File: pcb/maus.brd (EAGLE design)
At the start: 100 x 101 mm, 79 parts, among them IC1 AP1509-50SG-13, J1 SS-52300-001, Q2 BSS123, Q3 BSS123, Q4 BSS123, Q6 PMN30XPEA, Q7 PMN30XPEA, U2 CH340C, U4 LP3965EMP-3.3, U6 LM358DR, U69 ESP32-S2-WROOM

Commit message: replace old libraries
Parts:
- CR1: device shared:POWERSO-20_STM -> maus:POWERSO-20_STM
- D1: device SP0503BAHTG:SOT143 -> maus:SOT143
- D10, D11, D12, D16, D17, D18, D19, D8, YRMOM: device shared:RB068VWM100 -> maus:RB068VWM100
- IC1: device shared:SOIC127P600X175-8N -> maus:SOIC127P600X175-8N
- J1: device shared:SS52300001 -> maus:SS52300001
- JP1, JP4: device pinhead:1X06 -> maus:1X06
- JP5: device pinhead:1X10 -> maus:1X10
- L2: device shared:WE-PD_1260/1245/1280/121054 -> maus:WE-PD_1260/1245/1280/121054
- Q6, Q7: device mosfet:SOT95P255X110-6N -> maus:SOT95P255X110-6N
- SENSOR_FRONT, SENSOR_LEFT, SENSOR_RIGHT: device pinhead:1X03 -> maus:1X03
- U$2: device ICM-20948:ICM_20948-F -> maus:ICM_20948-F
- U$4: device xt60:XT60-UPRIGHT -> maus:XT60-UPRIGHT
- U2: device CH340C:SOIC127P600X180-16N -> maus:SOIC127P600X180-16N
- U4: device LP3965EMP-3.3:SOT150P696X180-5N -> maus:SOT150P696X180-5N
- U6: device LM358DR:SOIC127P610X175-8N -> maus:SOIC127P610X175-8N
- U69: device ESP32-S2-WROOM:XCVR_ESP32-S2-WROOM -> maus:XCVR_ESP32-S2-WROOM

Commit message: replace motor and sensor footprints
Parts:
- U$1: device shared:MOTOR_HALTERUNG -> maus:MOTOR_HALTERUNG
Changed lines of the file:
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@@
 <attribute name="VALUE" x="95.74" y="69.17" size="1.27" layer="27" rot="R270" align="center"/>
 </element>
-<element name="U$1" library="shared" package="MOTOR_HALTERUNG" value="" x="26" y="25" locked="yes" smashed="yes" rot="R90"/>
+<element name="U$1" library="maus" package="MOTOR_HALTERUNG" value="" x="26" y="25" locked="yes" smashed="yes" rot="R90"/>
 <element name="U$5" library="shared" package="MOTOR_HALTERUNG" value="" x="116" y="25" smashed="yes" rot="R90"/>
 <element name="U$6" library="shared" package="SENSOR_HALTERUNG" value="" x="116" y="77" smashed="yes" rot="R90"/>

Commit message: fixed some autorouter shit
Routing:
- net CLK: track 63.2 -> 36.3 mm, vias 0 -> 1
- net GND: track 838.0 -> 853.0 mm
- net MISO: track 53.3 -> 48.2 mm

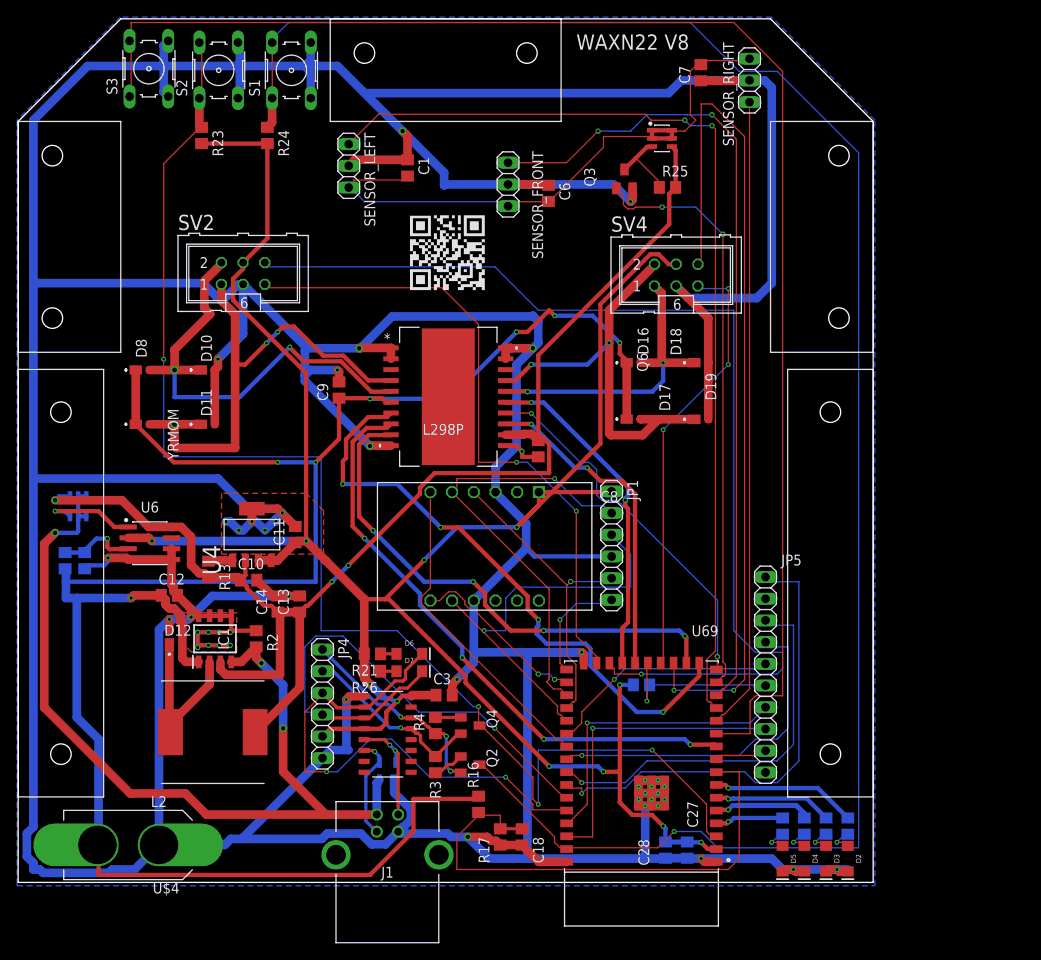
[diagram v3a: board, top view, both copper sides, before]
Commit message: set power tracks to (hopefully) sensible width
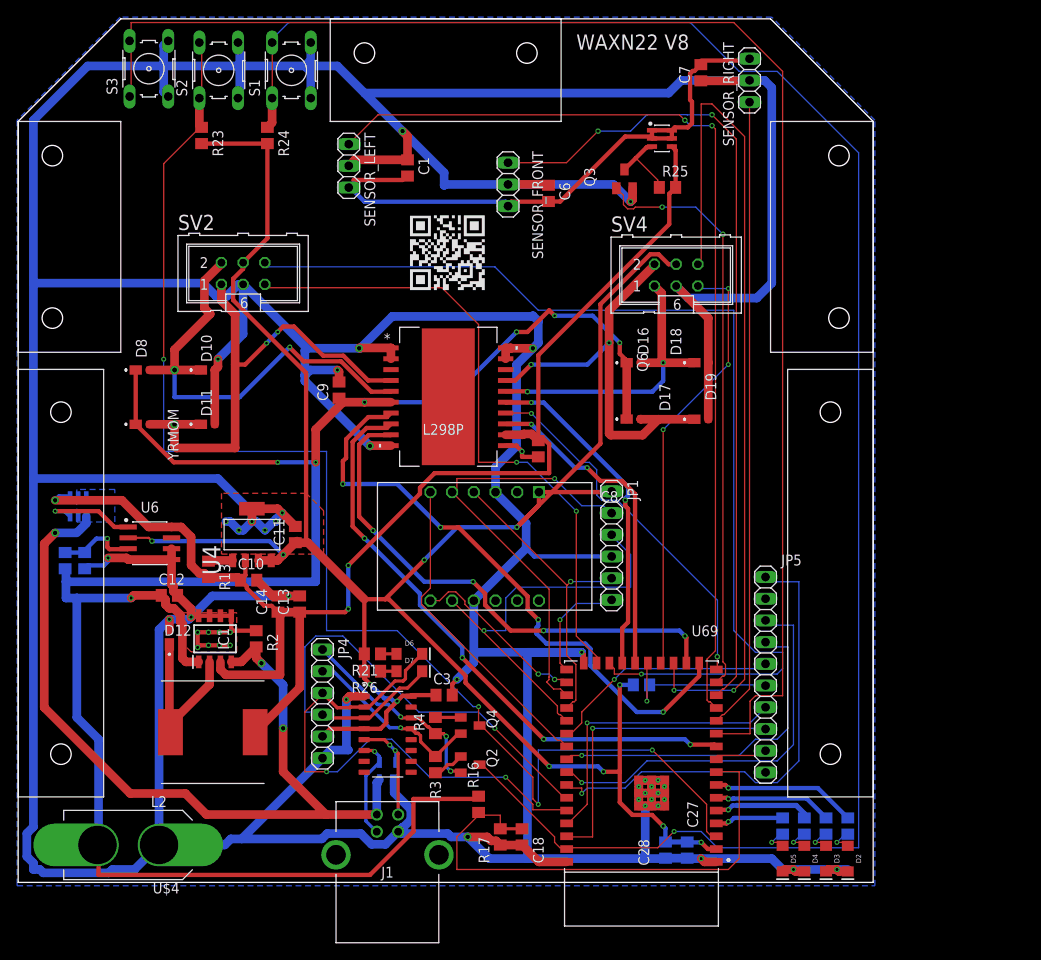
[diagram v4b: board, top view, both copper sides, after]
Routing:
- net +3V3: track 273.0 -> 269.2 mm
- net USB_VBUS: track 104.6 -> 100.8 mm
- net +5V: track 159.2 -> 162.2 mm
- added copper zone on layer 16, net USB_VBUS

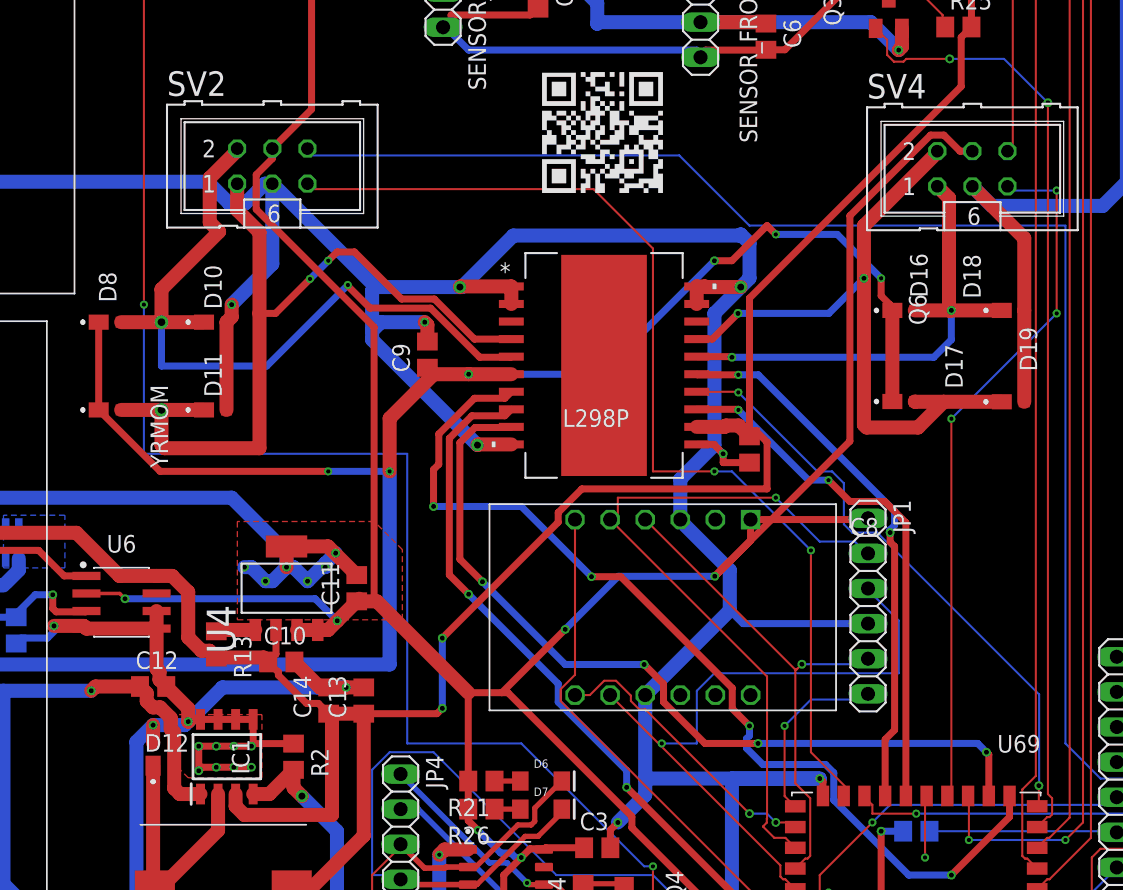
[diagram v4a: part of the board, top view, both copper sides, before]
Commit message: set motor track size 30mil (for ca. 700mA)
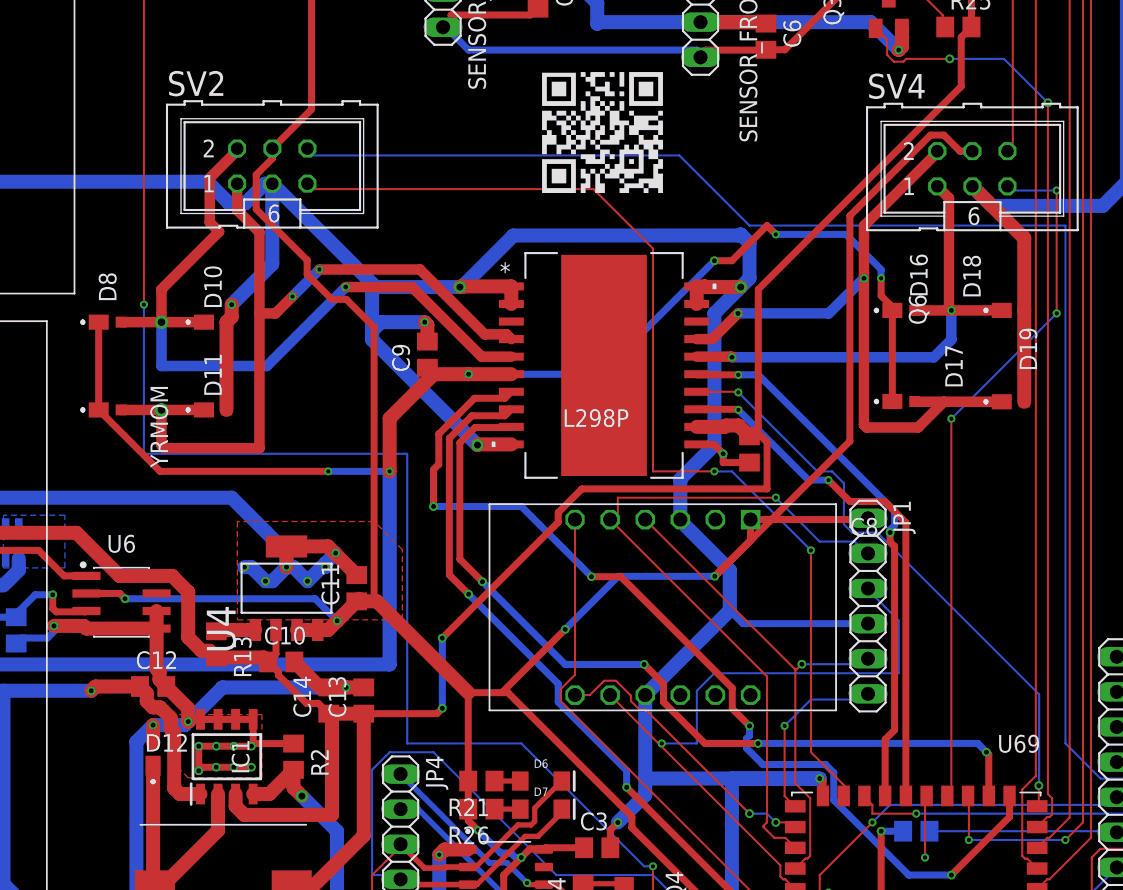
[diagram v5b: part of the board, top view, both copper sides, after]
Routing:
- net M1_M+: track 58.2 -> 57.2 mm
- net +3V3: track 269.2 -> 269.8 mm

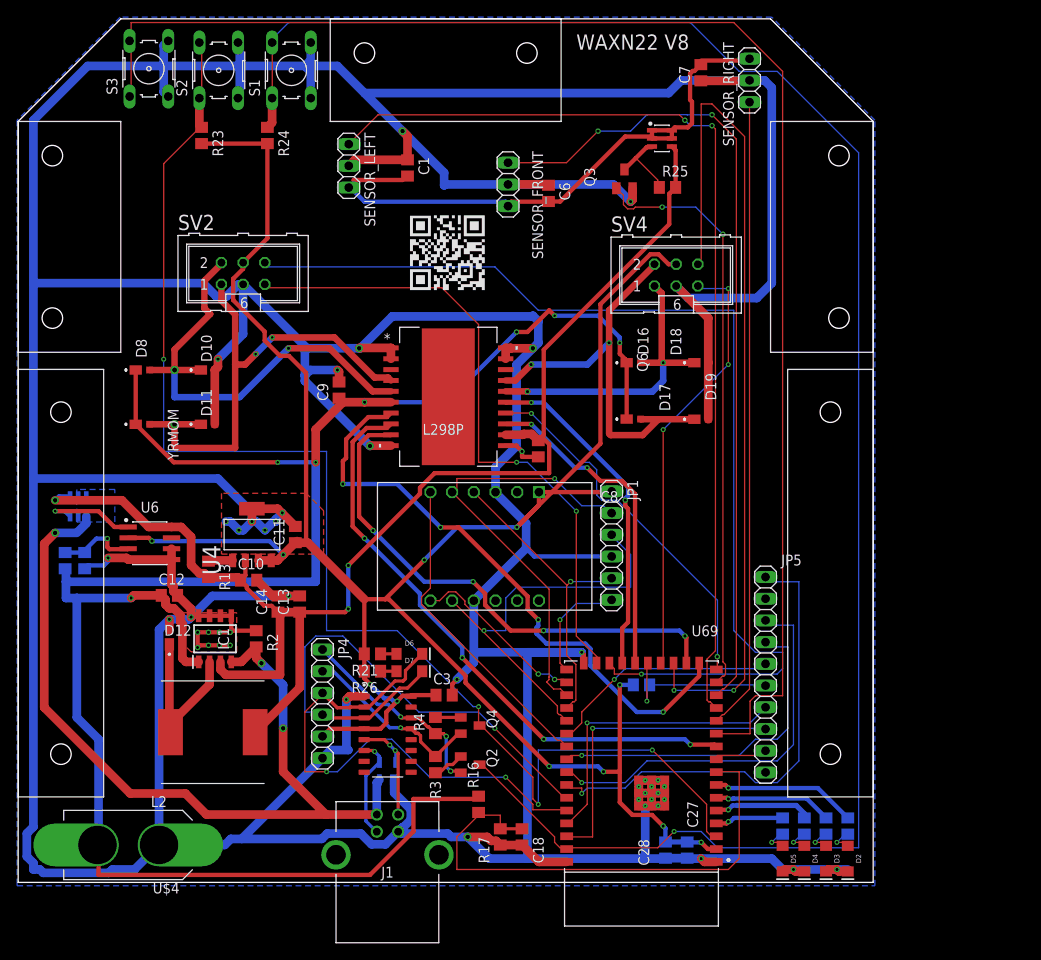
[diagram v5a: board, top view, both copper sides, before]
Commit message: Changed via sizes
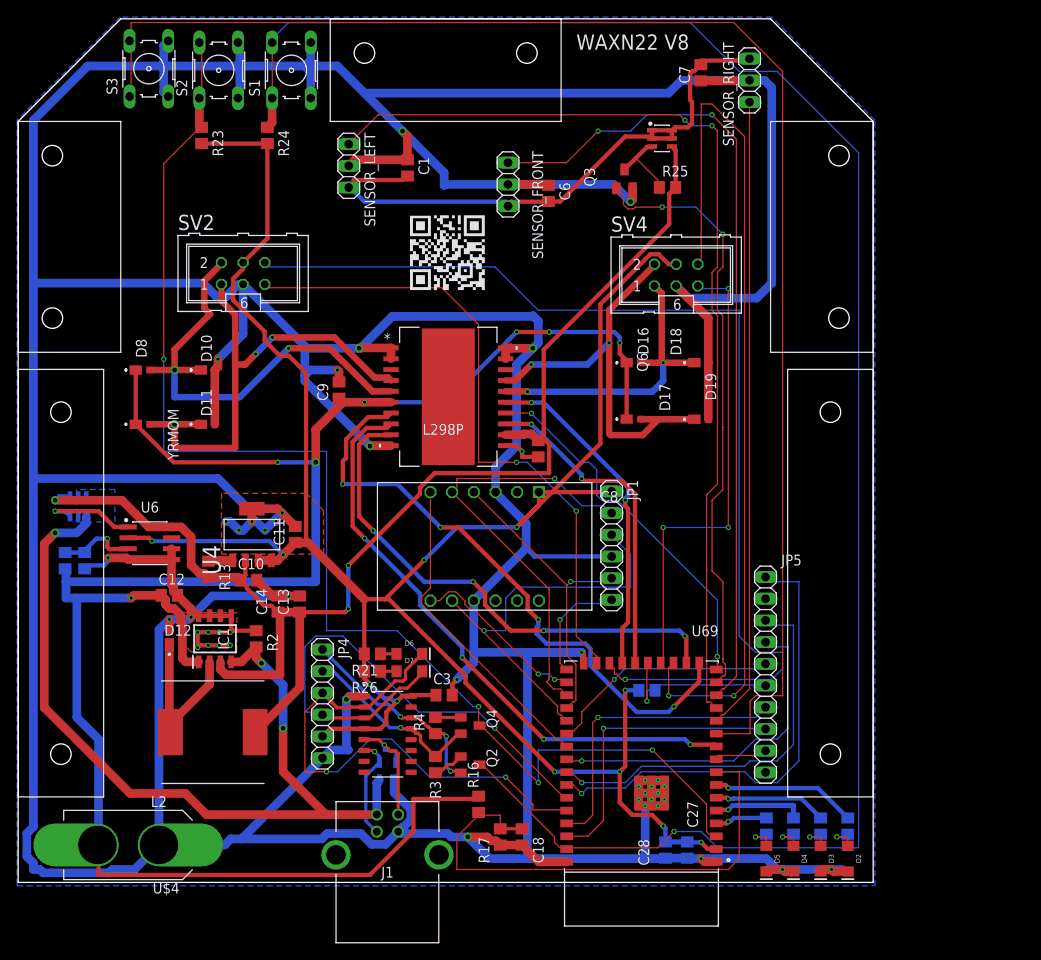
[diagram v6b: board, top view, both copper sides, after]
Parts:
- moved D5 1.91 mm to (103.5, 17.8)
- moved R20 1.91 mm to (103.5, 21.6)
- moved D4 1.27 mm to (106.7, 17.8)
- moved R19 1.27 mm to (106.7, 21.6)
- moved R28 0.90 mm to (89.5, 37.5)
- moved D3 0.63 mm to (109.9, 17.8)
- moved R18 0.63 mm to (109.9, 21.6)
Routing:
- net ESP32_IO0: track 159.1 -> 154.0 mm
- net ESP32_M2_CH_B: track 50.7 -> 55.2 mm
- net VBAT: track 242.2 -> 240.1 mm
- net ESP32_M2_CH_A: track 101.1 -> 103.2 mm
- net LED_DEBUG_4: track 8.03 -> 6.12 mm
- net D_P: track 13.2 -> 15.0 mm, vias 2 -> 1
- net SENSOR_EN: track 68.6 -> 70.2 mm
- net IO45: track 34.4 -> 35.8 mm
- net SENSOR_LEFT: track 113.7 -> 114.7 mm
- net ESP32_M1_CH_A: track 124.9 -> 125.8 mm
- net LED_DEBUG_3: track 11.5 -> 10.7 mm
- net IO46: track 36.0 -> 35.3 mm
- net LED_DEBUG_2: track 13.9 -> 13.2 mm
- net GND: track 852.5 -> 853.1 mm

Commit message: update vias and fix DRC issues
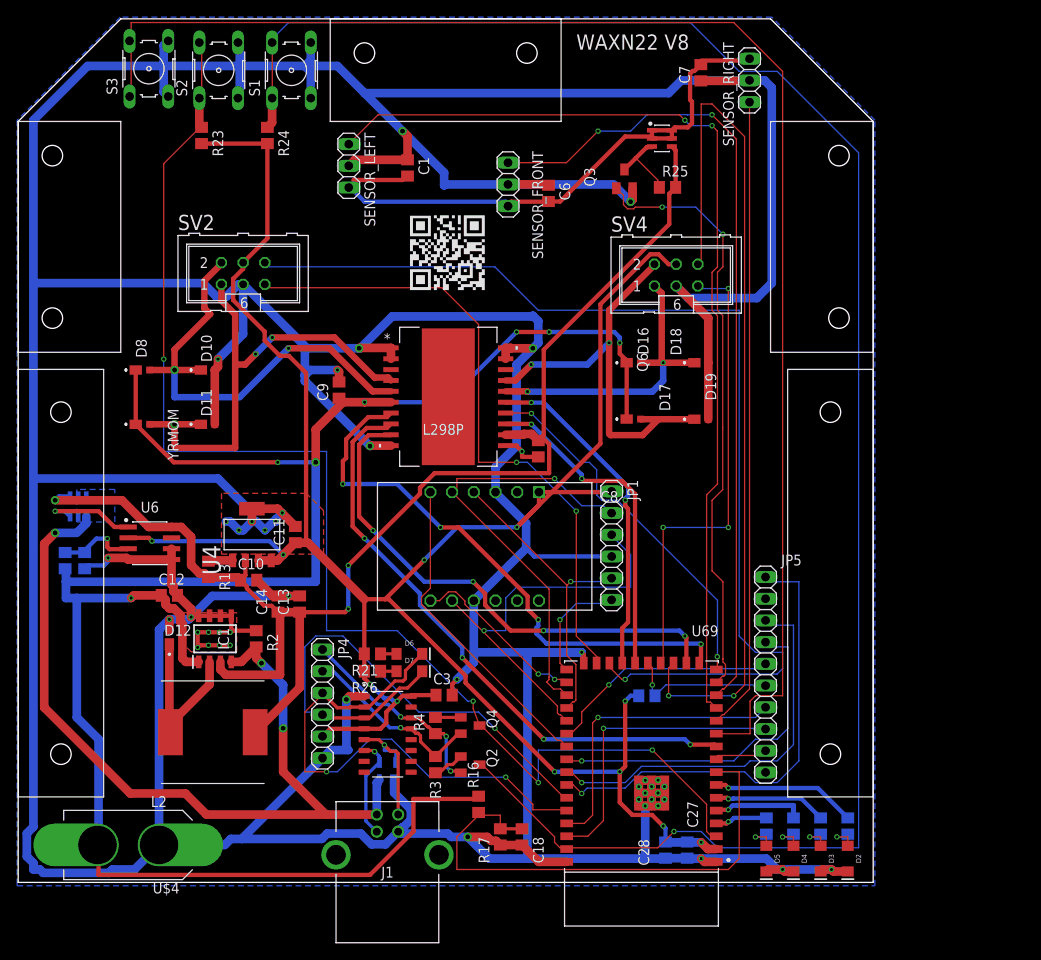
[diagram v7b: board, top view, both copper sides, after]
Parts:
- moved R28 0.64 mm to (89.5, 36.8)
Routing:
- net ESP32_M1_1: track 71.6 -> 66.0 mm
- net GND: track 853.1 -> 849.6 mm
- net IO18: track 20.0 -> 17.7 mm
- net +3V3: track 269.4 -> 268.2 mm
- net N$7: track 71.7 -> 70.8 mm
- net DRDY_A/G: track 56.2 -> 55.5 mm
- net IO45: track 35.8 -> 35.2 mm
- net IO46: track 35.3 -> 34.8 mm

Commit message: removed some long tracks on gnd plane
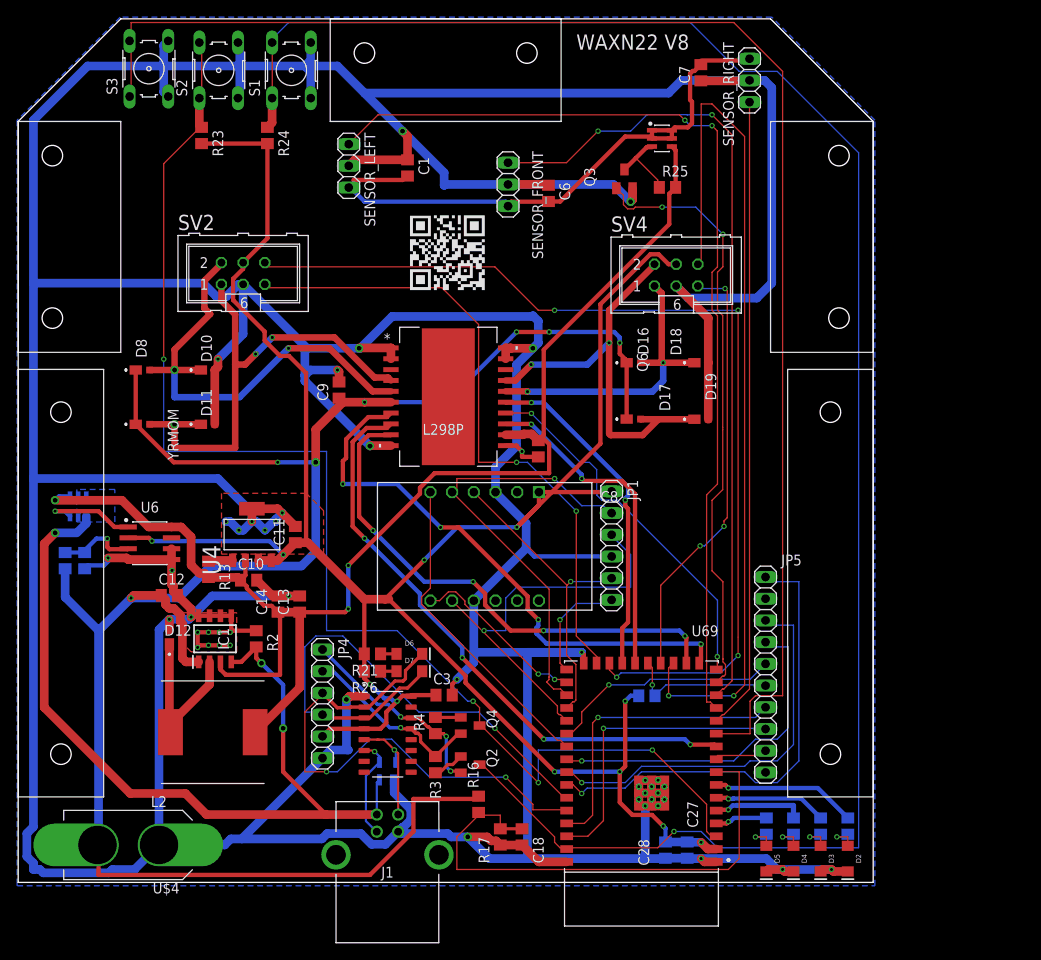
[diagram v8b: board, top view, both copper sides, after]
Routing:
- net VBAT: track 240.1 -> 229.7 mm
- net ESP32_M1_CH_A: track 125.6 -> 115.9 mm, vias 1 -> 4
- net ESP32_M2_CH_B: track 55.2 -> 51.4 mm
- net D_P: track 15.0 -> 13.5 mm
- net GND: vias 33 -> 34
